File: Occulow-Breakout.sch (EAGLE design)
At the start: 12 parts

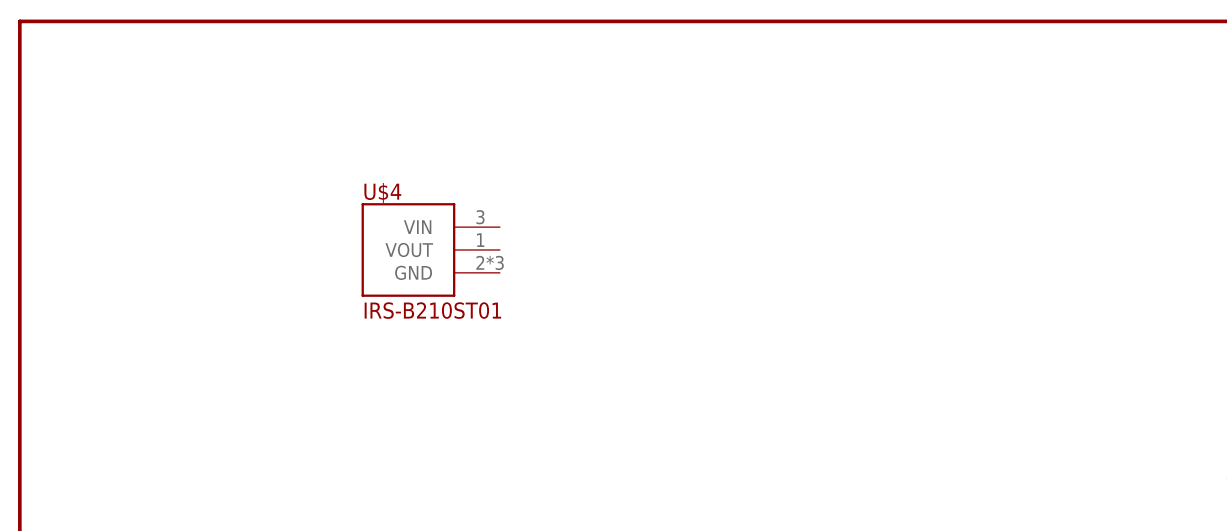
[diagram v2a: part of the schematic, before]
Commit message: PIR power circuit
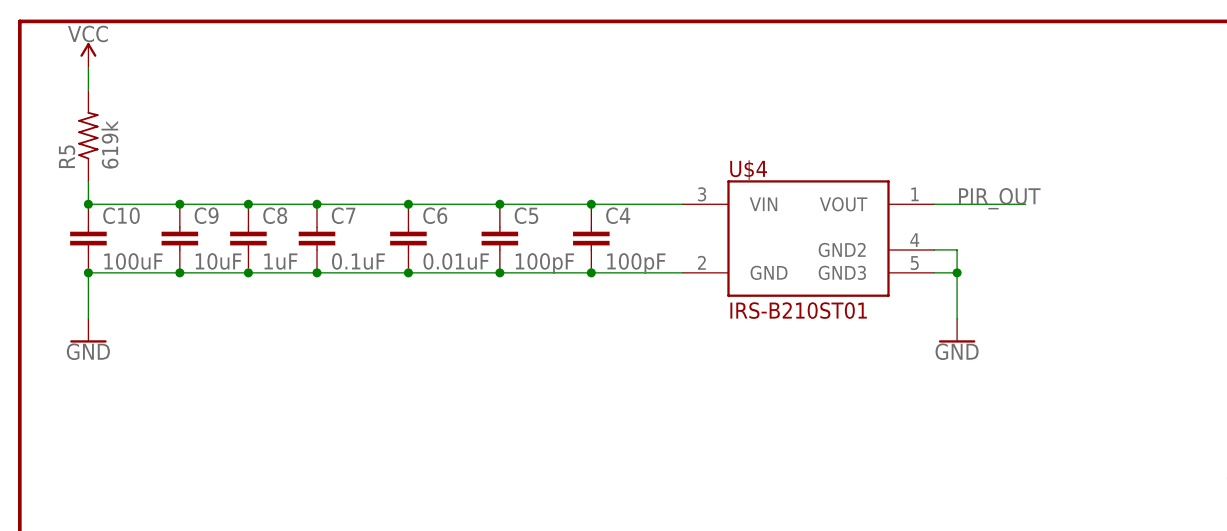
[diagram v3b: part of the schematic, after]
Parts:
- added C10: 100uF, rcl:C-EUC1206
- added C4, C5: 100pF, rcl:C-EUC1206
- added C6: 0.01uF, rcl:C-EUC1206
- added C7: 0.1uF, rcl:C-EUC1206
- added C8: 1uF, rcl:C-EUC1206
- added C9: 10uF, rcl:C-EUC1206
- added R5: 619k, resistor:R-US_R1206
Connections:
- new net N$5: C10.1, C4.1, C5.1, C6.1, C7.1, C8.1, C9.1, R5.1, U$4.VIN
- new net PIR_OUT: U$4.VOUT
- net GND: now also C10.2, C4.2, C5.2, C6.2, C7.2, C8.2, C9.2, U$4.GND, U$4.GND2, U$4.GND3
- net VCC: now also R5.2
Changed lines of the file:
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@@
 <part name="GND8" library="SparkFun-PowerSymbols" deviceset="GND" device=""/>
 <part name="U$4" library="PIR" deviceset="IRS-B210ST01" device=""/>
+<part name="GND9" library="SparkFun-PowerSymbols" deviceset="GND" device=""/>
+<part name="C4" library="rcl" deviceset="C-EU" device="C1206" value="100pF"/>
+<part name="C5" library="rcl" deviceset="C-EU" device="C1206" value="100pF"/>
+<part name="C6" library="rcl" deviceset="C-EU" device="C1206" value="0.01uF"/>
+<part name="C7" library="rcl" deviceset="C-EU" device="C1206" value="0.1uF"/>
+<part name="C8" library="rcl" deviceset="C-EU" device="C1206" value="1uF"/>
+<part name="C9" library="rcl" deviceset="C-EU" device="C1206" value="10uF"/>
+<part name="C10" library="rcl" deviceset="C-EU" device="C1206" value="100uF"/>
+<part name="GND10" library="SparkFun-PowerSymbols" deviceset="GND" device=""/>
+<part name="SUPPLY3" library="SparkFun-PowerSymbols" deviceset="VCC" device=""/>
+<part name="R5" library="resistor" deviceset="R-US_" device="R1206" value="619k"/>
 </parts>
 <sheets>
@@
 <instance part="GND7" gate="1" x="350.52" y="83.82"/>
 <instance part="GND8" gate="1" x="297.18" y="83.82"/>
-<instance part="U$4" gate="G$1" x="205.74" y="154.94"/>
+<instance part="U$4" gate="G$1" x="246.38" y="157.48"/>
+<instance part="GND9" gate="1" x="266.7" y="144.78"/>
+<instance part="C4" gate="G$1" x="226.06" y="157.48"/>
+<instance part="C5" gate="G$1" x="215.9" y="157.48"/>
+<instance part="C6" gate="G$1" x="205.74" y="157.48"/>
+<instance part="C7" gate="G$1" x="195.58" y="157.48"/>
+<instance part="C8" gate="G$1" x="187.96" y="157.48"/>
+<instance part="C9" gate="G$1" x="180.34" y="157.48"/>
+<instance part="C10" gate="G$1" x="170.18" y="157.48"/>
+<instance part="GND10" gate="1" x="170.18" y="144.78"/>
+<instance part="SUPPLY3" gate="G$1" x="170.18" y="175.26"/>
+<instance part="R5" gate="G$1" x="170.18" y="167.64" rot="R90"/>
 </instances>
 <busses>
@@
 <wire x1="243.84" y1="55.88" x2="248.92" y2="55.88" width="0.1524" layer="91"/>
 <junction x="248.92" y="55.88"/>
+</segment>
+<segment>
+<pinref part="R5" gate="G$1" pin="2"/>
+<pinref part="SUPPLY3" gate="G$1" pin="VCC"/>
+<wire x1="170.18" y1="172.72" x2="170.18" y2="175.26" width="0.1524" layer="91"/>
 </segment>
 </net>
@@
 <junction x="297.18" y="93.98"/>
 </segment>
+<segment>
+<pinref part="U$4" gate="G$1" pin="GND2"/>
+<pinref part="GND9" gate="1" pin="GND"/>
+<wire x1="264.16" y1="154.94" x2="266.7" y2="154.94" width="0.1524" layer="91"/>
+<wire x1="266.7" y1="154.94" x2="266.7" y2="152.4" width="0.1524" layer="91"/>
+<pinref part="U$4" gate="G$1" pin="GND3"/>
+<wire x1="266.7" y1="152.4" x2="266.7" y2="147.32" width="0.1524" layer="91"/>
+<wire x1="264.16" y1="152.4" x2="266.7" y2="152.4" width="0.1524" layer="91"/>
+<junction x="266.7" y="152.4"/>
+</segment>
+<segment>
+<pinref part="U$4" gate="G$1" pin="GND"/>
+<pinref part="C4" gate="G$1" pin="2"/>
+<wire x1="236.22" y1="152.4" x2="226.06" y2="152.4" width="0.1524" layer="91"/>
+<pinref part="C5" gate="G$1" pin="2"/>
+<wire x1="226.06" y1="152.4" x2="215.9" y2="152.4" width="0.1524" layer="91"/>
+<junction x="226.06" y="152.4"/>
+<pinref part="C6" gate="G$1" pin="2"/>
+<wire x1="215.9" y1="152.4" x2="205.74" y2="152.4" width="0.1524" layer="91"/>
+<junction x="215.9" y="152.4"/>
+<pinref part="C7" gate="G$1" pin="2"/>
+<wire x1="205.74" y1="152.4" x2="195.58" y2="152.4" width="0.1524" layer="91"/>
+<junction x="205.74" y="152.4"/>
+<pinref part="C8" gate="G$1" pin="2"/>
+<wire x1="195.58" y1="152.4" x2="187.96" y2="152.4" width="0.1524" layer="91"/>
+<junction x="195.58" y="152.4"/>
+<pinref part="C9" gate="G$1" pin="2"/>
+<wire x1="187.96" y1="152.4" x2="180.34" y2="152.4" width="0.1524" layer="91"/>
+<junction x="187.96" y="152.4"/>
+<pinref part="C10" gate="G$1" pin="2"/>
+<wire x1="180.34" y1="152.4" x2="170.18" y2="152.4" width="0.1524" layer="91"/>
+<junction x="180.34" y="152.4"/>
+<pinref part="GND10" gate="1" pin="GND"/>
+<wire x1="170.18" y1="152.4" x2="170.18" y2="147.32" width="0.1524" layer="91"/>
+<junction x="170.18" y="152.4"/>
+</segment>
 </net>
 <net name="N$2" class="0">
@@
 </segment>
 </net>
+<net name="N$5" class="0">
+<segment>
+<pinref part="U$4" gate="G$1" pin="VIN"/>
+<pinref part="C4" gate="G$1" pin="1"/>
+<wire x1="236.22" y1="160.02" x2="226.06" y2="160.02" width="0.1524" layer="91"/>
+<pinref part="C5" gate="G$1" pin="1"/>
+<wire x1="226.06" y1="160.02" x2="215.9" y2="160.02" width="0.1524" layer="91"/>
+<junction x="226.06" y="160.02"/>
+<pinref part="C6" gate="G$1" pin="1"/>
+<wire x1="215.9" y1="160.02" x2="205.74" y2="160.02" width="0.1524" layer="91"/>
+<junction x="215.9" y="160.02"/>
+<pinref part="C7" gate="G$1" pin="1"/>
+<wire x1="205.74" y1="160.02" x2="195.58" y2="160.02" width="0.1524" layer="91"/>
+<junction x="205.74" y="160.02"/>
+<pinref part="C8" gate="G$1" pin="1"/>
+<wire x1="195.58" y1="160.02" x2="187.96" y2="160.02" width="0.1524" layer="91"/>
+<junction x="195.58" y="160.02"/>
+<pinref part="C9" gate="G$1" pin="1"/>
+<wire x1="187.96" y1="160.02" x2="180.34" y2="160.02" width="0.1524" layer="91"/>
+<junction x="187.96" y="160.02"/>
+<pinref part="C10" gate="G$1" pin="1"/>
+<wire x1="180.34" y1="160.02" x2="170.18" y2="160.02" width="0.1524" layer="91"/>
+<junction x="180.34" y="160.02"/>
+<pinref part="R5" gate="G$1" pin="1"/>
+<wire x1="170.18" y1="160.02" x2="170.18" y2="162.56" width="0.1524" layer="91"/>
+<junction x="170.18" y="160.02"/>
+</segment>
+</net>
+<net name="PIR_OUT" class="0">
+<segment>
+<pinref part="U$4" gate="G$1" pin="VOUT"/>
+<wire x1="264.16" y1="160.02" x2="274.32" y2="160.02" width="0.1524" layer="91"/>
+<label x="266.7" y="160.02" size="1.778" layer="95"/>
+</segment>
+</net>

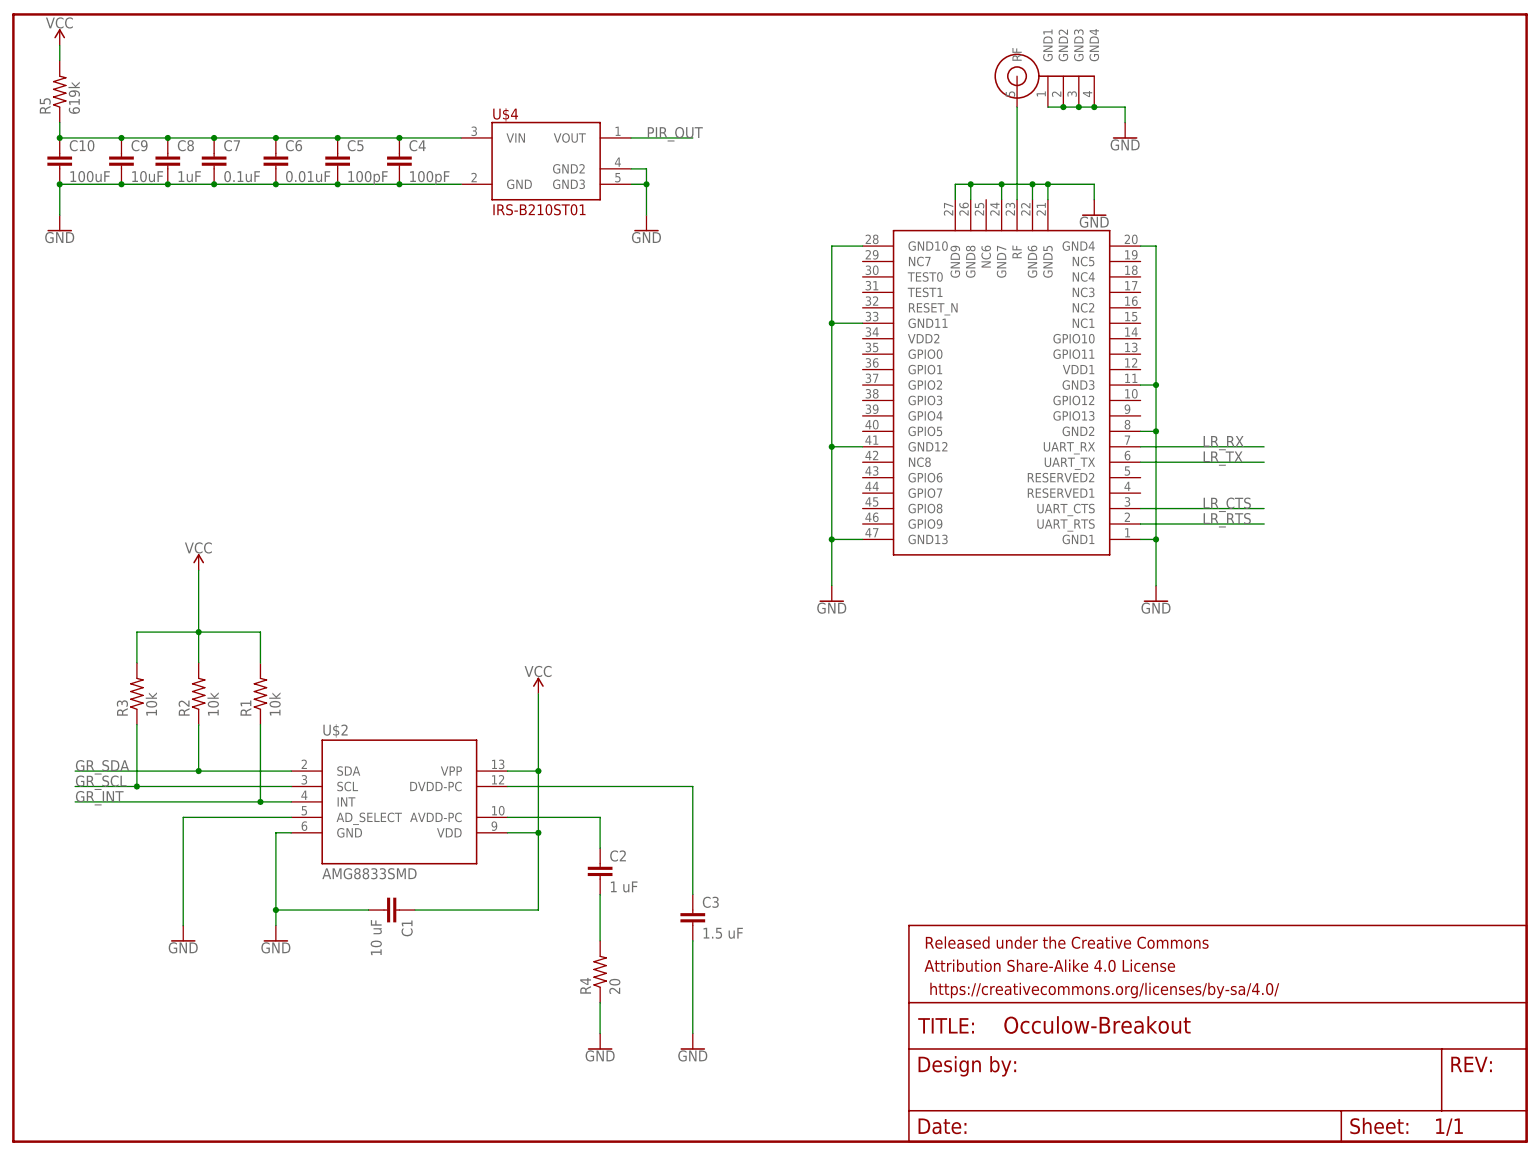
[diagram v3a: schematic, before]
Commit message: Separate vcc's, headers for all
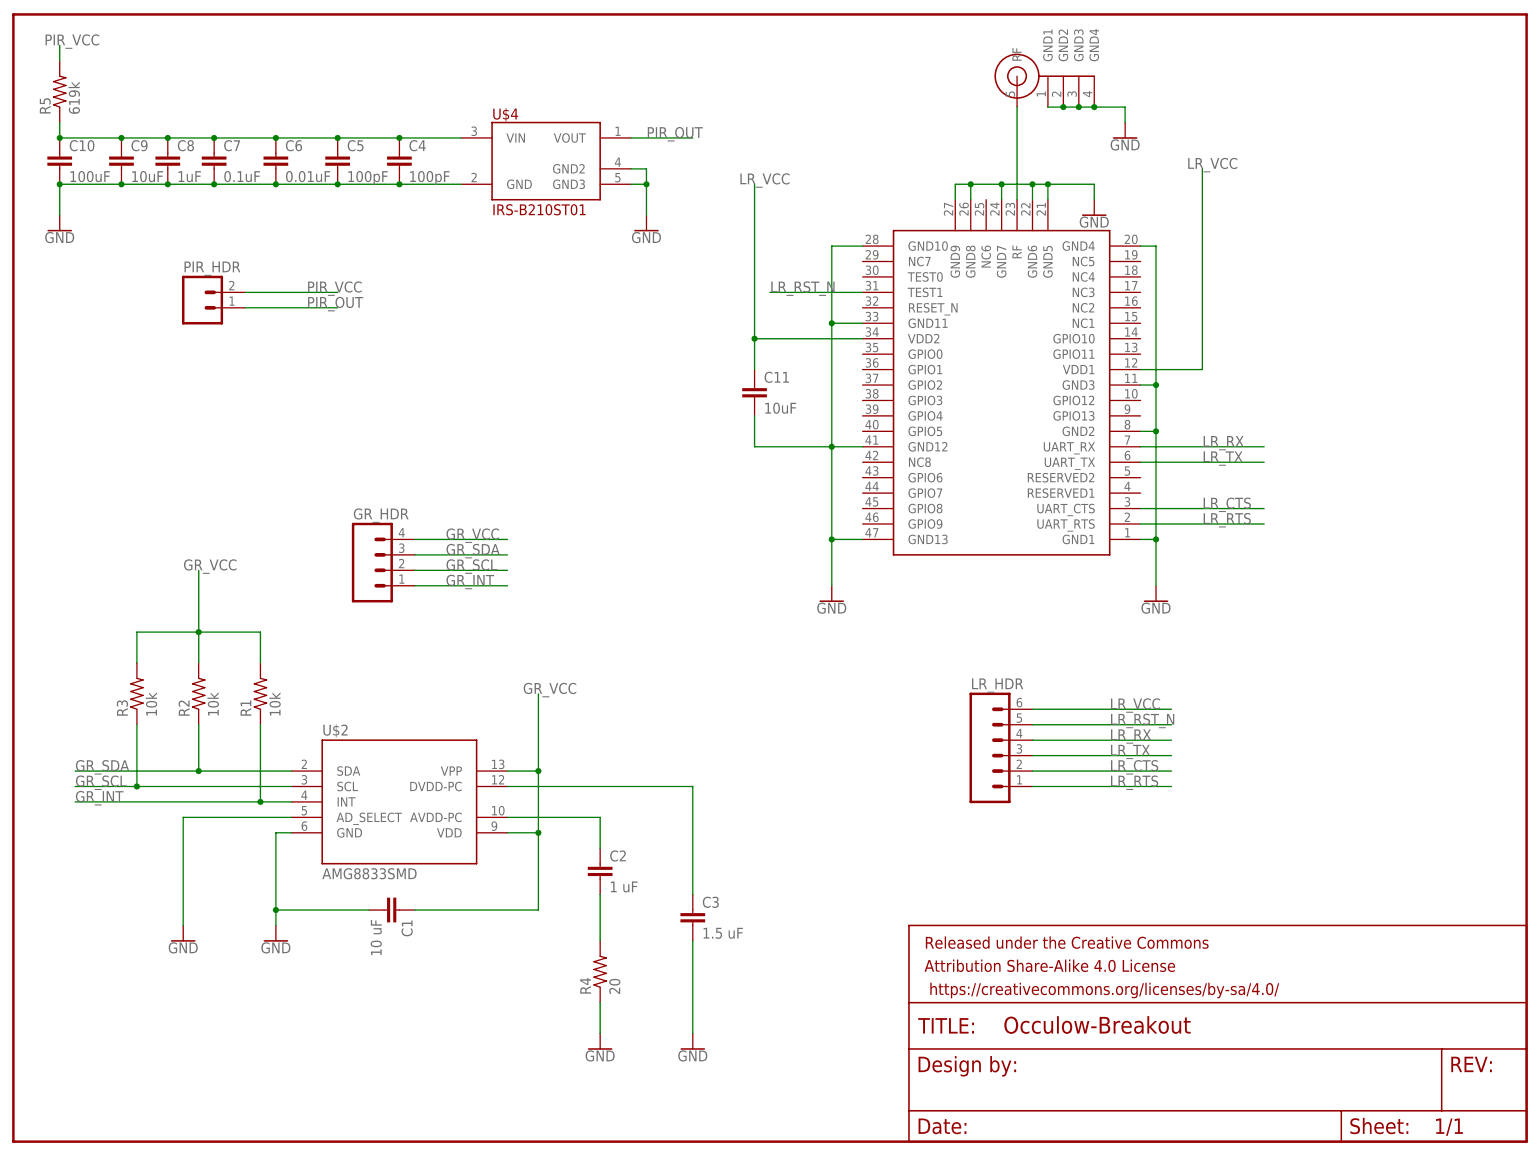
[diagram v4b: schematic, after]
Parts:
- added C11: 10uF, rcl:C-EUC1206
- added GR_HDR: (no value), con-amp-quick:M04
- added LR_HDR: (no value), con-amp-quick:M06
- added PIR_HDR: (no value), con-amp-quick:M02
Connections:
- removed net VCC: C1.1, R1.2, R2.2, R3.2, R5.2, U$2.VDD, U$2.VPP
- new net GR_VCC: C1.1, GR_HDR.4, R1.2, R2.2, R3.2, U$2.VDD, U$2.VPP
- new net LR_RST_N: LR_HDR.5, U$1.TEST1
- new net LR_VCC: C11.1, LR_HDR.6, U$1.VDD1, U$1.VDD2
- new net PIR_VCC: PIR_HDR.2, R5.2
- net GND: now also C11.2
- net GR_INT: now also GR_HDR.1
- net GR_SCL: now also GR_HDR.2
- net GR_SDA: now also GR_HDR.3
- net LR_CTS: now also LR_HDR.2
- net LR_RTS: now also LR_HDR.1
- net LR_RX: now also LR_HDR.4
- net LR_TX: now also LR_HDR.3
- net PIR_OUT: now also PIR_HDR.1
